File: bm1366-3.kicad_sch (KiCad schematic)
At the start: 50 parts, among them U14 BM1366_mode0, U5 MCP1824T-1202E, U6 MCP1824T-0802E

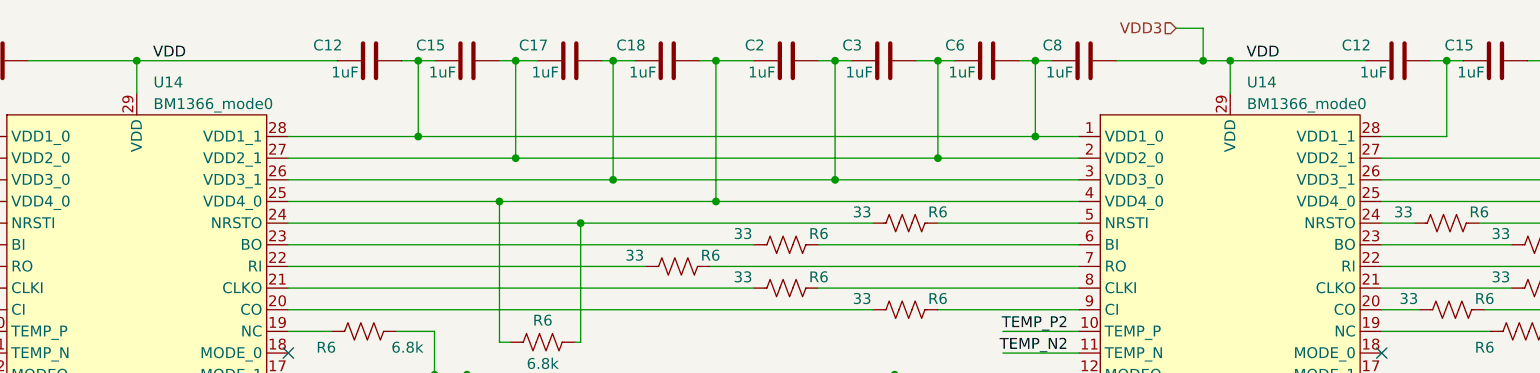
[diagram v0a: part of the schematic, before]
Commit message: cleanup parts and symbol libraries. added TMP1075
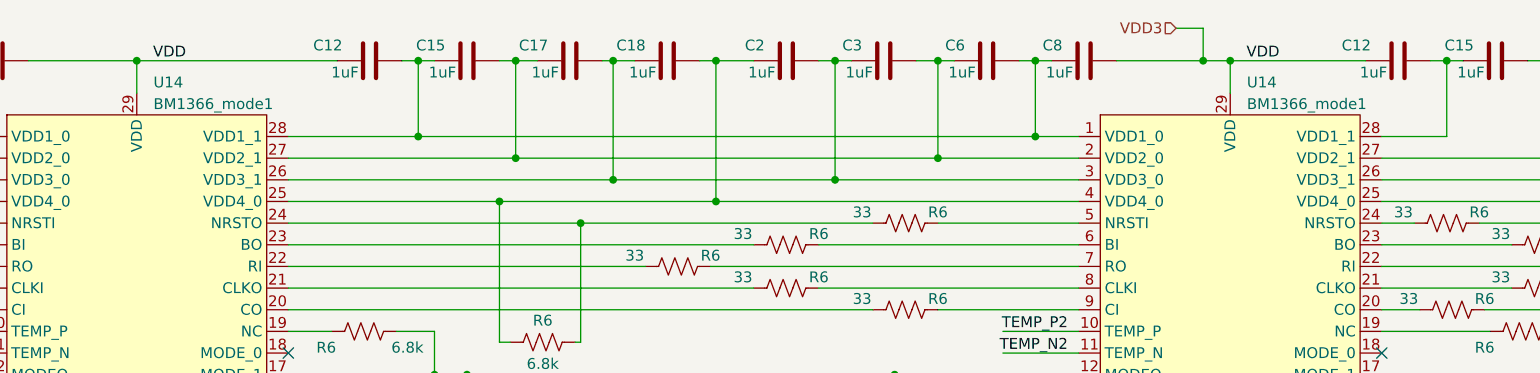
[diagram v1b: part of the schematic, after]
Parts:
- U14: value BM1366_mode0 -> BM1366_mode1; symbol Bitaxe:BM1366_mode1 -> bitaxe:BM1366_mode1
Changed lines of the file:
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@@
     )
   )
-  (symbol (lib_id "Bitaxe:BM1366_mode1") (at 201.295 74.93 0) (unit 1)
+  (symbol (lib_id "bitaxe:BM1366_mode1") (at 201.295 74.93 0) (unit 1)
     (in_bom yes) (on_board yes) (dnp no) (fields_autoplaced)
     (property "Reference" "U14" (at 203.2509 50.8 0)
       (effects (font (size 1.27 1.27)) (justify left))
     )
-    (property "Value" "BM1366_mode0" (at 203.2509 53.34 0)
+    (property "Value" "BM1366_mode1" (at 203.2509 53.34 0)
       (effects (font (size 1.27 1.27)) (justify left))
     )
@@
     )
   )
-  (symbol (lib_id "Bitaxe:BM1366_mode1") (at 73.025 74.93 0) (unit 1)
+  (symbol (lib_id "bitaxe:BM1366_mode1") (at 73.025 74.93 0) (unit 1)
     (in_bom yes) (on_board yes) (dnp no) (fields_autoplaced)
     (property "Reference" "U14" (at 74.9809 50.8 0)
       (effects (font (size 1.27 1.27)) (justify left))
     )
-    (property "Value" "BM1366_mode0" (at 74.9809 53.34 0)
+    (property "Value" "BM1366_mode1" (at 74.9809 53.34 0)
       (effects (font (size 1.27 1.27)) (justify left))
     )

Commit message: moved all custom symbols and footprints to the bitaxe library
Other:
- title: (none) -> bitaxeUltraHex
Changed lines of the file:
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@@
 (kicad_sch (version 20230121) (generator eeschema)
   (paper "A")
+  (title_block
+    (title "bitaxeUltraHex")
+    (date "2023-06-11")
+    (rev "1")
+  )
   (junction (at 115.57 64.77) (diameter 0) (color 0 0 0 0)
   )

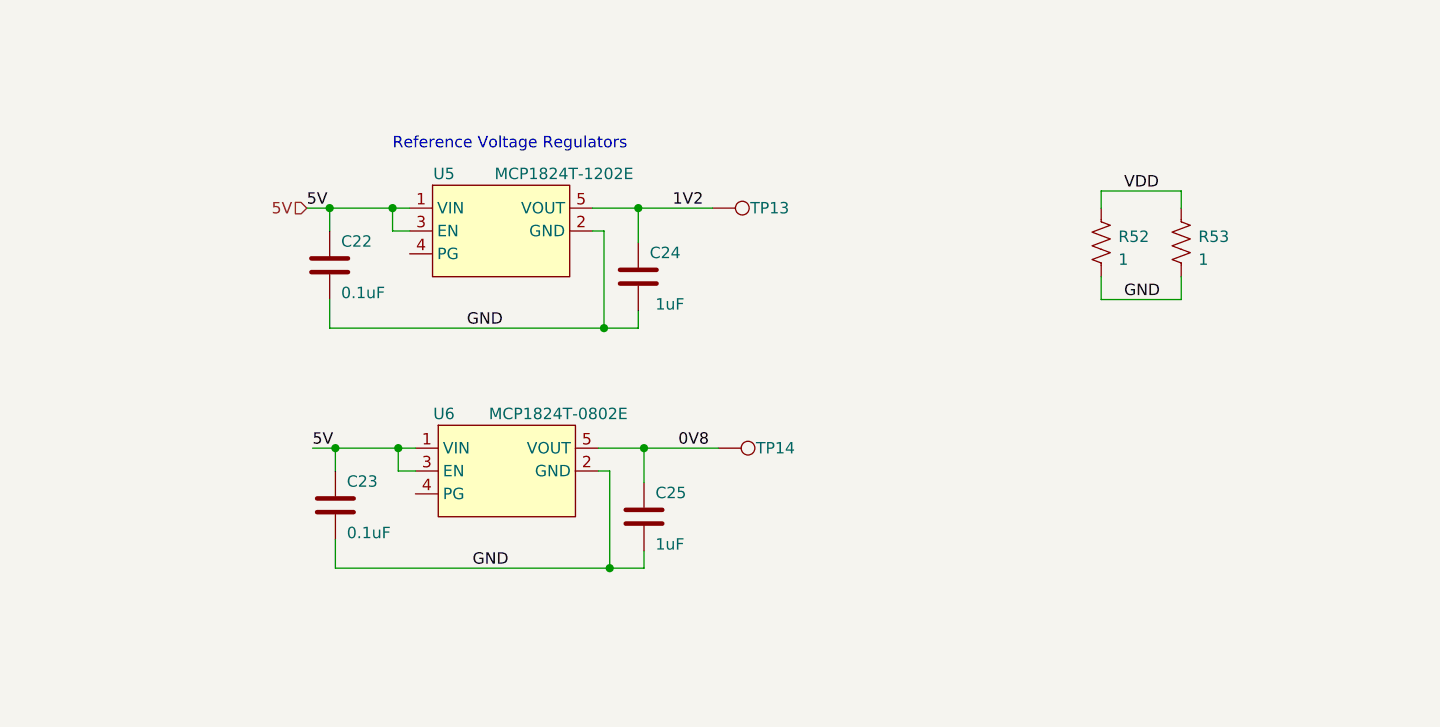
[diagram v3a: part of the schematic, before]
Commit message: Replace reference voltage regulators with new one
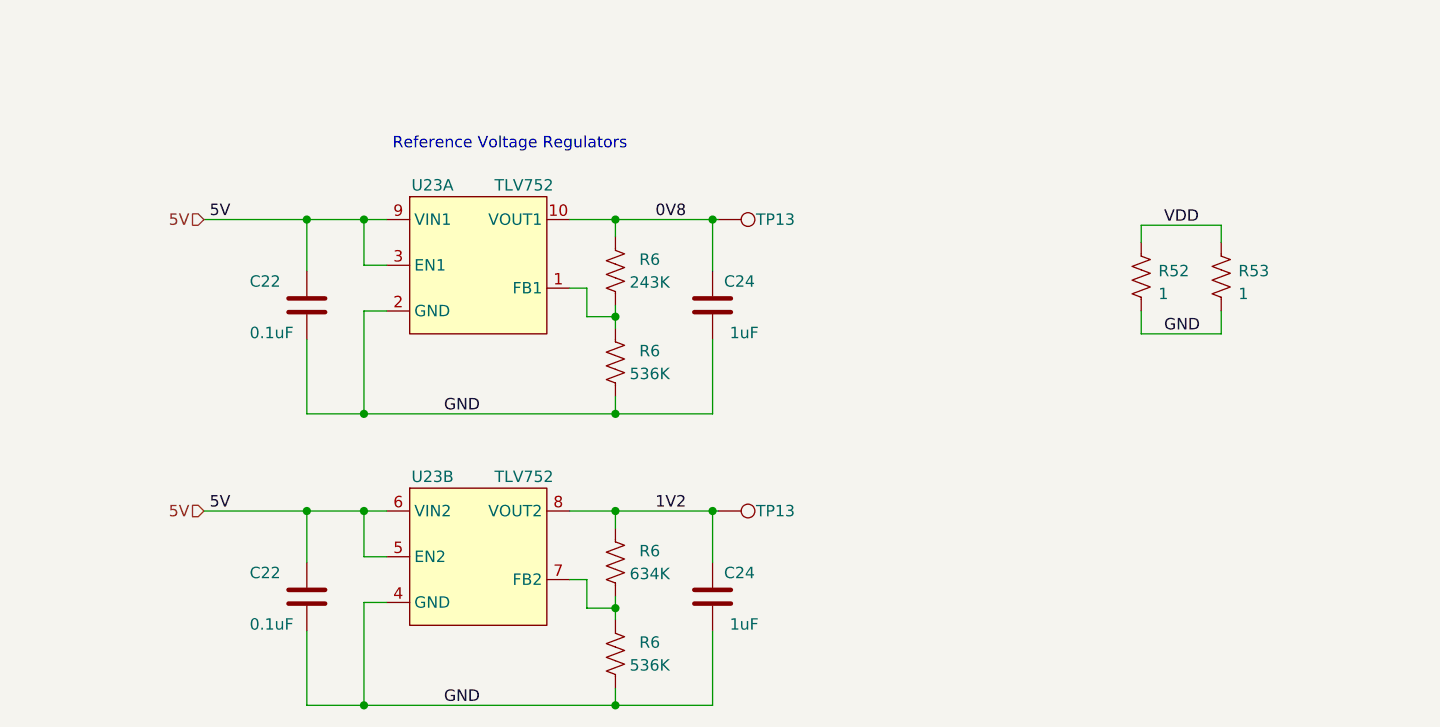
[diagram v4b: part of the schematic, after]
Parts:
- removed C22, C23: 0.1uF, Capacitor_SMD:C_0402_1005Metric, symbol Device:C
- removed C24, C25: 1uF, Capacitor_SMD:C_0402_1005Metric, symbol Device:C
- removed TP13, TP14: TestPoint, TestPoint:TestPoint_Pad_D1.5mm, symbol Connector:TestPoint
- removed U5: MCP1824T-1202E, Package_TO_SOT_SMD:SOT-23-5, symbol bitaxe:MCP1824
- removed U6: MCP1824T-0802E, Package_TO_SOT_SMD:SOT-23-5, symbol bitaxe:MCP1824
- added C22 (x2): 0.1uF, Capacitor_SMD:C_0402_1005Metric, symbol Device:C
- added C24 (x2): 1uF, Capacitor_SMD:C_0402_1005Metric, symbol Device:C
- added R6 (x2): 536K, Resistor_SMD:R_0402_1005Metric, symbol Device:R_US
- added R6: 634K, Resistor_SMD:R_0402_1005Metric, symbol Device:R_US
- added R6: 243K, Resistor_SMD:R_0402_1005Metric, symbol Device:R_US
- added TP13 (x2): TestPoint, TestPoint:TestPoint_Pad_D1.5mm, symbol Connector:TestPoint
- added U23: TLV752, Package_SON:WSON-10-1EP_2.5x2.5mm_P0.5mm_EP1.2x2mm, symbol bitaxe:TLV752
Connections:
- net 0V8: now also C24.1, R6.2, TP13.1, U23.10 (VOUT1)
- net 1V2: now also C24.1, R6.2, TP13.1, U23.8 (VOUT2)
- net 5V: now also C22.1, C22.1, U23.3 (EN1), U23.5 (EN2), U23.6 (VIN2), U23.9 (VIN1)
- net GND3: now also C22.2, C22.2, C24.2, C24.2, R6.1, R6.1, U23.2 (GND), U23.4 (GND)
- new net: R6.1, R6.2, U23.1 (FB1)
- new net: R6.1, R6.2, U23.7 (FB2)
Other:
- moved on the sheet: R52, R53

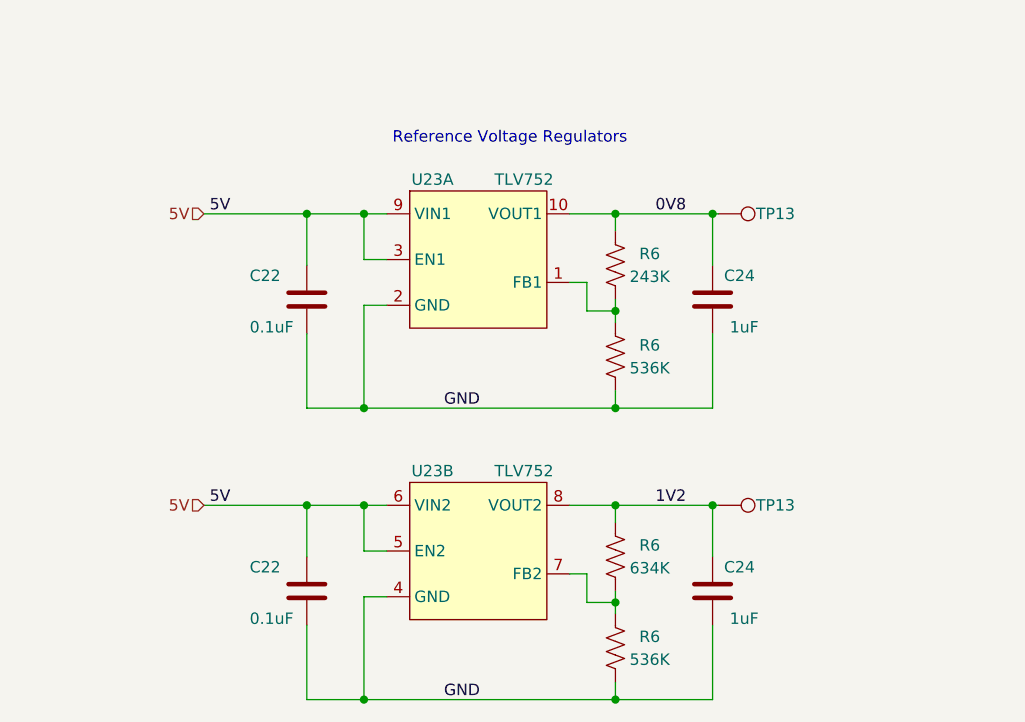
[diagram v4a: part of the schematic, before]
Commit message: switch voltage reference regulators to ADP170, reannotate
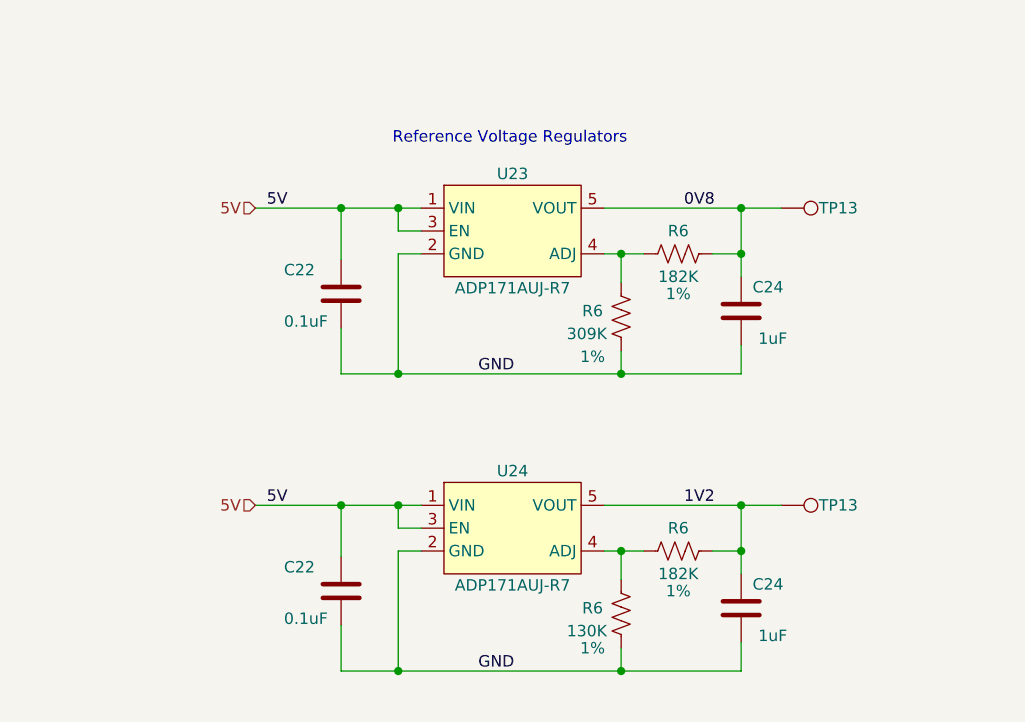
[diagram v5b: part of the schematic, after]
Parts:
- removed C22 (x2): 0.1uF, Capacitor_SMD:C_0402_1005Metric, symbol Device:C
- removed C24 (x2): 1uF, Capacitor_SMD:C_0402_1005Metric, symbol Device:C
- removed R6 (x2): 536K, Resistor_SMD:R_0402_1005Metric, symbol Device:R_US
- removed R6: 634K, Resistor_SMD:R_0402_1005Metric, symbol Device:R_US
- removed R6: 243K, Resistor_SMD:R_0402_1005Metric, symbol Device:R_US
- removed TP13 (x2): TestPoint, TestPoint:TestPoint_Pad_D1.5mm, symbol Connector:TestPoint
- removed U23: TLV752, Package_SON:WSON-10-1EP_2.5x2.5mm_P0.5mm_EP1.2x2mm, symbol bitaxe:TLV752
- added C22 (x2): 0.1uF, Capacitor_SMD:C_0402_1005Metric, symbol Device:C
- added C24 (x2): 1uF, Capacitor_SMD:C_0402_1005Metric, symbol Device:C
- added R6: 130K, Resistor_SMD:R_0402_1005Metric, symbol Device:R_US
- added R6 (x2): 182K, Resistor_SMD:R_0402_1005Metric, symbol Device:R_US
- added R6: 309K, Resistor_SMD:R_0402_1005Metric, symbol Device:R_US
- added TP13 (x2): TestPoint, TestPoint:TestPoint_Pad_D1.5mm, symbol Connector:TestPoint
- added U23, U24: ADP171AUJ-R7, Package_TO_SOT_SMD:TSOT-23-5, symbol bitaxe:ADP171AUJ-R7
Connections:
- net 0V8: now also C24.1, R6.1, TP13.1, U23.5 (VOUT)
- net 1V2: now also C24.1, R6.1, TP13.1, U24.5 (VOUT)
- net 5V: now also C22.1, C22.1, U23.1 (VIN), U23.3 (EN), U24.1 (VIN), U24.3 (EN)
- net GND3: now also C22.2, C22.2, C24.2, C24.2, R6.1, R6.1, U23.2 (GND), U24.2 (GND)
- new net: R6.2, R6.2, U23.4 (ADJ)
- new net: R6.2, R6.2, U24.4 (ADJ)

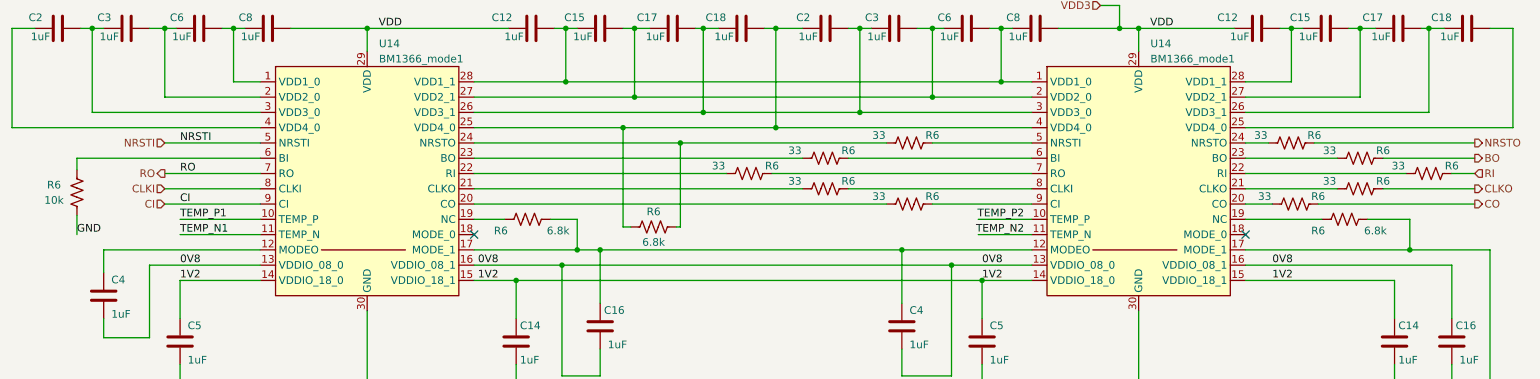
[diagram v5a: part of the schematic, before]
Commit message: added enclosure edge cuts. added heatsink outline. changed the two middle voltage domain ASICs to mode 0 so the data lines can snake through all 6 chips.
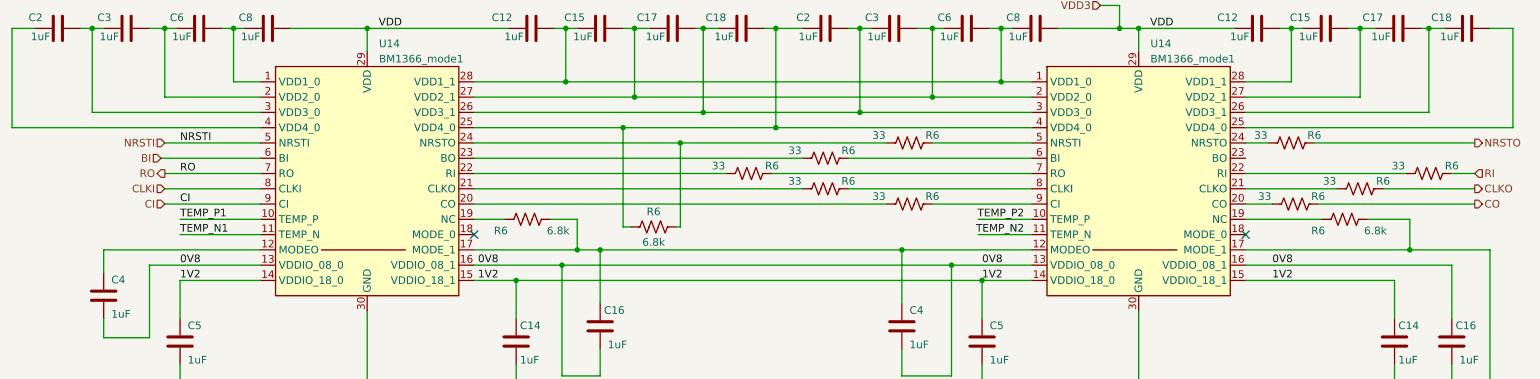
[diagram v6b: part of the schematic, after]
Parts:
- removed R6: 10k, Resistor_SMD:R_0402_1005Metric, symbol Device:R_US
- removed R6: 33, Resistor_SMD:R_0402_1005Metric, symbol Device:R_US
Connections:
- net BI: now reaches U14.6 (BI)
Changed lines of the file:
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@@
-    (stroke (width 0) (type default))
-  )
-  (wire (pts (xy 241.935 69.85) (xy 257.175 69.85))
     (stroke (width 0) (type default))
   )
@@
     (stroke (width 0) (type default))
   )
-  (wire (pts (xy 24.765 79.375) (xy 24.765 82.55))
-    (stroke (width 0) (type default))
-  )
   (wire (pts (xy 167.005 48.26) (xy 168.91 48.26))
     (stroke (width 0) (type default))
@@
     (stroke (width 0) (type default))
   )
-  (wire (pts (xy 24.765 69.85) (xy 24.765 71.755))
-    (stroke (width 0) (type default))
-  )
   (wire (pts (xy 149.225 135.89) (xy 149.225 137.795))
     (stroke (width 0) (type default))
@@
     (stroke (width 0) (type default))
   )
+  (wire (pts (xy 38.735 69.85) (xy 55.245 69.85))
+    (stroke (width 0) (type default))
+  )
   (wire (pts (xy 95.885 153.035) (xy 82.55 153.035))
     (stroke (width 0) (type default))
@@
     (stroke (width 0) (type default))
   )
-  (wire (pts (xy 24.765 69.85) (xy 55.245 69.85))
-    (stroke (width 0) (type default))
-  )
   (wire (pts (xy 73.025 95.25) (xy 73.025 109.22))
     (stroke (width 0) (type default))
@@
   )
   (wire (pts (xy 140.335 137.795) (xy 140.335 135.89))
-    (stroke (width 0) (type default))
-  )
-  (wire (pts (xy 219.075 69.85) (xy 234.315 69.85))
     (stroke (width 0) (type default))
   )
@@
     (effects (font (size 1.27 1.27)) (justify left bottom))
   )
-  (label "GND" (at 24.765 82.55 0) (fields_autoplaced)
-    (effects (font (size 1.27 1.27)) (justify left bottom))
-  )
   (hierarchical_label "NRSTO" (shape output) (at 257.175 67.31 0) (fields_autoplaced)
     (effects (font (size 1.27 1.27)) (justify left))
@@
     (effects (font (size 1.27 1.27)) (justify left))
   )
-  (hierarchical_label "BO" (shape output) (at 257.175 69.85 0) (fields_autoplaced)
-    (effects (font (size 1.27 1.27)) (justify left))
-  )
   (hierarchical_label "NRSTI" (shape input) (at 39.37 67.31 180) (fields_autoplaced)
     (effects (font (size 1.27 1.27)) (justify right))
@@
   (hierarchical_label "RI" (shape input) (at 257.175 72.39 0) (fields_autoplaced)
     (effects (font (size 1.27 1.27)) (justify left))
+  )
+  (hierarchical_label "BI" (shape input) (at 38.735 69.85 180) (fields_autoplaced)
+    (effects (font (size 1.27 1.27)) (justify right))
   )
   (hierarchical_label "CLKI" (shape input) (at 39.37 74.93 180) (fields_autoplaced)
@@
         (path "/e63e39d7-6ac0-4ffd-8aa3-1841a4541b55/e182566a-9202-4486-8792-212410a9233c"
           (reference "C105") (unit 1)
-        )
-      )
-    )
-  )
-  (symbol (lib_id "Device:R_US") (at 24.765 75.565 180) (unit 1)
-    (in_bom yes) (on_board yes) (dnp no)
-    (property "Reference" "R6" (at 20.955 74.295 0)
-      (effects (font (size 1.27 1.27)))
-    )
-    (property "Value" "10k" (at 20.955 76.835 0)
-      (effects (font (size 1.27 1.27)))
-    )
-    (property "Footprint" "Resistor_SMD:R_0402_1005Metric" (at 23.749 75.311 90)
-      (effects (font (size 1.27 1.27)) hide)
-    )
-    (property "Datasheet" "~" (at 24.765 75.565 0)
-      (effects (font (size 1.27 1.27)) hide)
-    )
-    (property "DK" "" (at 24.765 75.565 0)
-      (effects (font (size 1.27 1.27)) hide)
-    )
-    (property "PARTNO" "" (at 24.765 75.565 0)
-      (effects (font (size 1.27 1.27)) hide)
-    )
-    (pin "1")
-    (pin "2")
-    (instances
-      (project "bm1397"
-        (path "/5ffa02c9-1f90-4b06-abee-1fc0c47a0c88"
-          (reference "R6") (unit 1)
-        )
-      )
-      (project "bitaxeUltraHex"
-        (path "/e63e39d7-6ac0-4ffd-8aa3-1841a4541b55/4cf9c075-d009-4c35-9949-adda70ae20c7"
-          (reference "R16") (unit 1)
-        )
-        (path "/e63e39d7-6ac0-4ffd-8aa3-1841a4541b55/831c2d7c-1b0c-48f0-8d88-f1b4f08c2544"
-          (reference "R35") (unit 1)
-        )
-        (path "/e63e39d7-6ac0-4ffd-8aa3-1841a4541b55/e182566a-9202-4486-8792-212410a9233c"
-          (reference "R59") (unit 1)
         )
       )
@@
         )
       )
-    )
-  )
-  (symbol (lib_id "Device:R_US") (at 238.125 69.85 90) (unit 1)
-    (in_bom yes) (on_board yes) (dnp no)
-    (property "Reference" "R6" (at 241.935 68.58 90)
-      (effects (font (size 1.27 1.27)))
-    )
-    (property "Value" "33" (at 233.045 68.58 90)
-      (effects (font (size 1.27 1.27)))
-    )
-    (property "Footprint" "Resistor_SMD:R_0402_1005Metric" (at 238.379 68.834 90)
-      (effects (font (size 1.27 1.27)) hide)
-    )
-    (property "Datasheet" "~" (at 238.125 69.85 0)
-      (effects (font (size 1.27 1.27)) hide)
-    )
-    (property "DK" "" (at 238.125 69.85 0)
-      (effects (font (size 1.27 1.27)) hide)
-    )
-    (property "PARTNO" "" (at 238.125 69.85 0)
-      (effects (font (size 1.27 1.27)) hide)
-    )
-    (pin "1")
-    (pin "2")
-    (instances
-      (project "bm1397"
-        (path "/5ffa02c9-1f90-4b06-abee-1fc0c47a0c88"
-          (reference "R6") (unit 1)
-        )
-      )
-      (project "bitaxeUltraHex"
-        (path "/e63e39d7-6ac0-4ffd-8aa3-1841a4541b55/4cf9c075-d009-4c35-9949-adda70ae20c7"
-          (reference "R29") (unit 1)
-        )
-        (path "/e63e39d7-6ac0-4ffd-8aa3-1841a4541b55/831c2d7c-1b0c-48f0-8d88-f1b4f08c2544"
-          (reference "R47") (unit 1)
-        )
-        (path "/e63e39d7-6ac0-4ffd-8aa3-1841a4541b55/e182566a-9202-4486-8792-212410a9233c"
-          (reference "R76") (unit 1)
-        )
-      )
